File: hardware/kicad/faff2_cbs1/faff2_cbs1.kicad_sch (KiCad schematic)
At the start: 0 parts

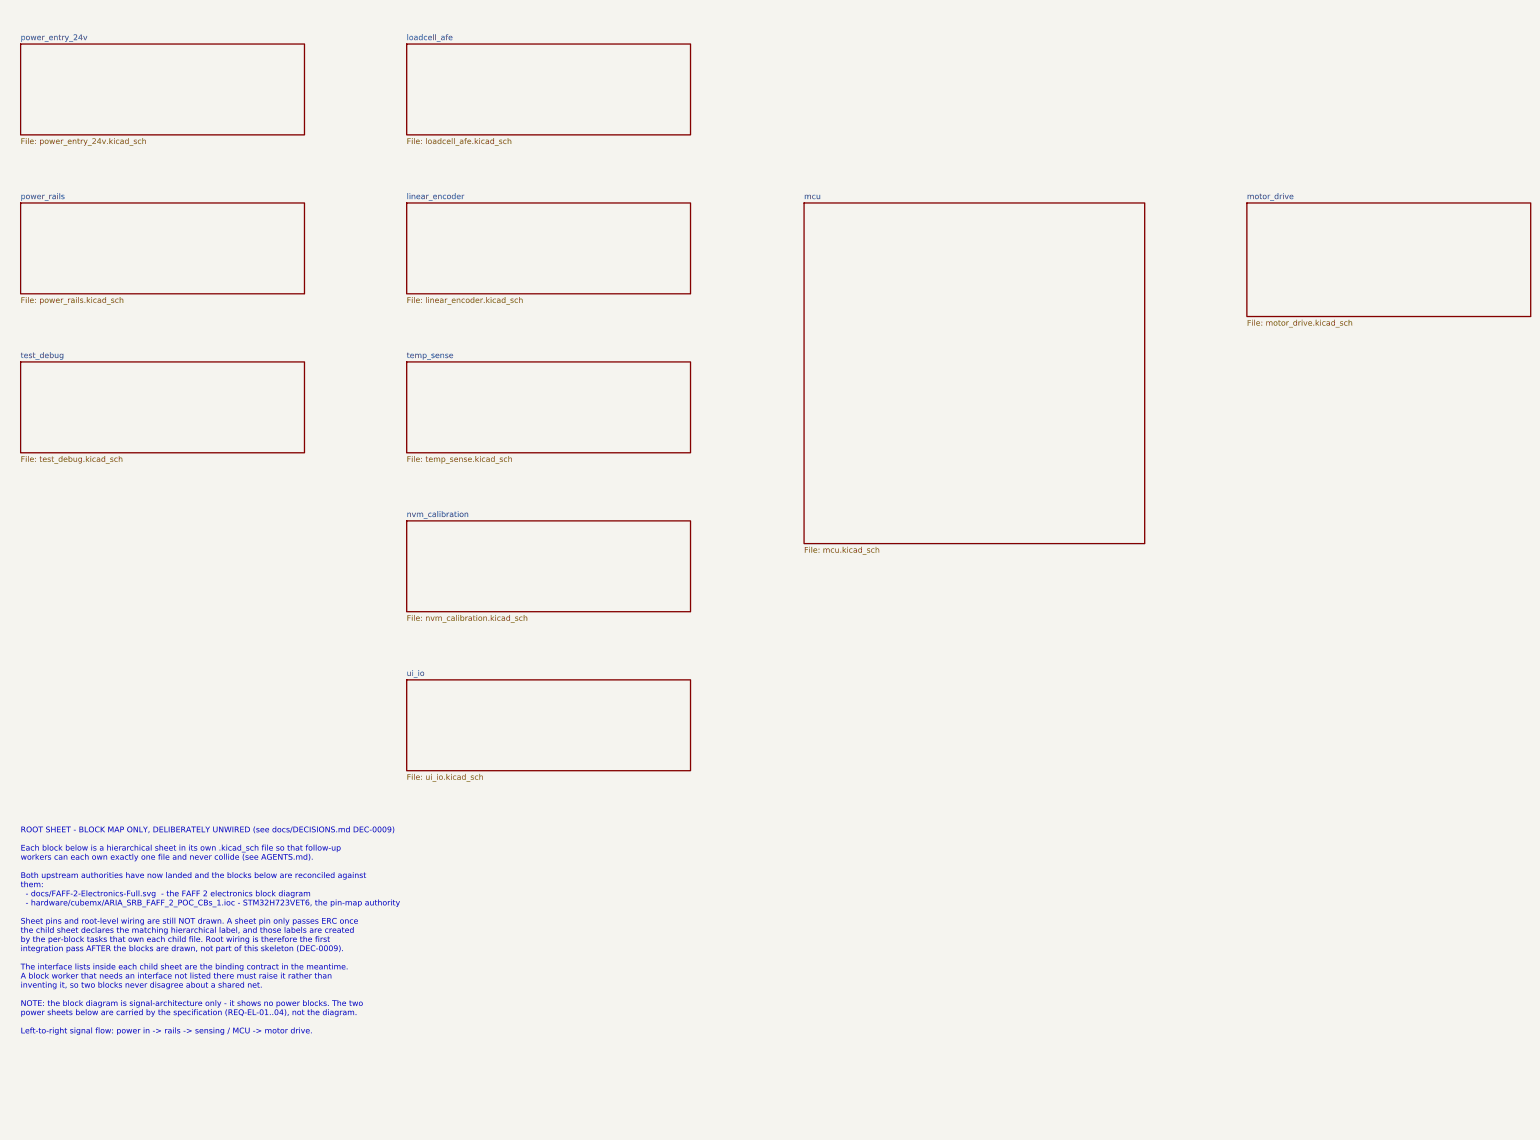
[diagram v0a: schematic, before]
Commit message: integrate: wire the root sheet - 113 sheet pins, 70 wires, ERC 0/0
Closes DEC-0009. Every net that crosses a block boundary is now drawn on
the root sheet: one sheet pin per hierarchical label a child declares,
each on a wire. Nothing on the root connects by name.

The layout is the block diagram of docs/FAFF-2-Electronics-Full.svg read
left to right - 24 V in top left, sensing and user I/O down the left
column, the MCU in the middle, motor drive on the right. Each peer
block's pin rows are aligned with the mcu rows they face, so all 48
mcu-to-peer nets are single straight wires with no bends and no
crossings.

Two topologies needed care:

  * power_entry_24v fans out to three different places. Its pins sit on
    a 5.08 mm pitch and the three routes are nested - V24_LOGIC straight
    across to power_rails, +24V_SW peeling down and running over the top
    of the mcu block to motor_drive, V24_MON dropping inside it - so no
    two cross.
  * the shared SPI2 CONFIG bus is tapped once per wire between
    motor_drive and temp_sense, which is why temp_sense sits under
    motor_drive rather than in the sensor column. The three taps and the
    ADS1120_nCS run are nested the same way: four junctions, zero
    crossings.

motor_drive declared CONFIG_SPI_MISO an output while temp_sense declared
it tri_state - the reconciliation actuator-sch-afe.md asked for at
integration. Both are tri_state now: three devices share that wire and
each drives it only while its own chip select is low.

Verification, whole project, nothing suppressed:
  ERC --severity-all          0 errors, 0 warnings (was 194 violations)
  netlist                     409 components, no duplicate references,
                              311 -> 253 nets, exactly the 58 merges the
                              113 pins over 55 net names predict
  overlap checker             root sheet clean; the 11 findings left in
                              linear_encoder / loadcell_afe / temp_sense
                     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
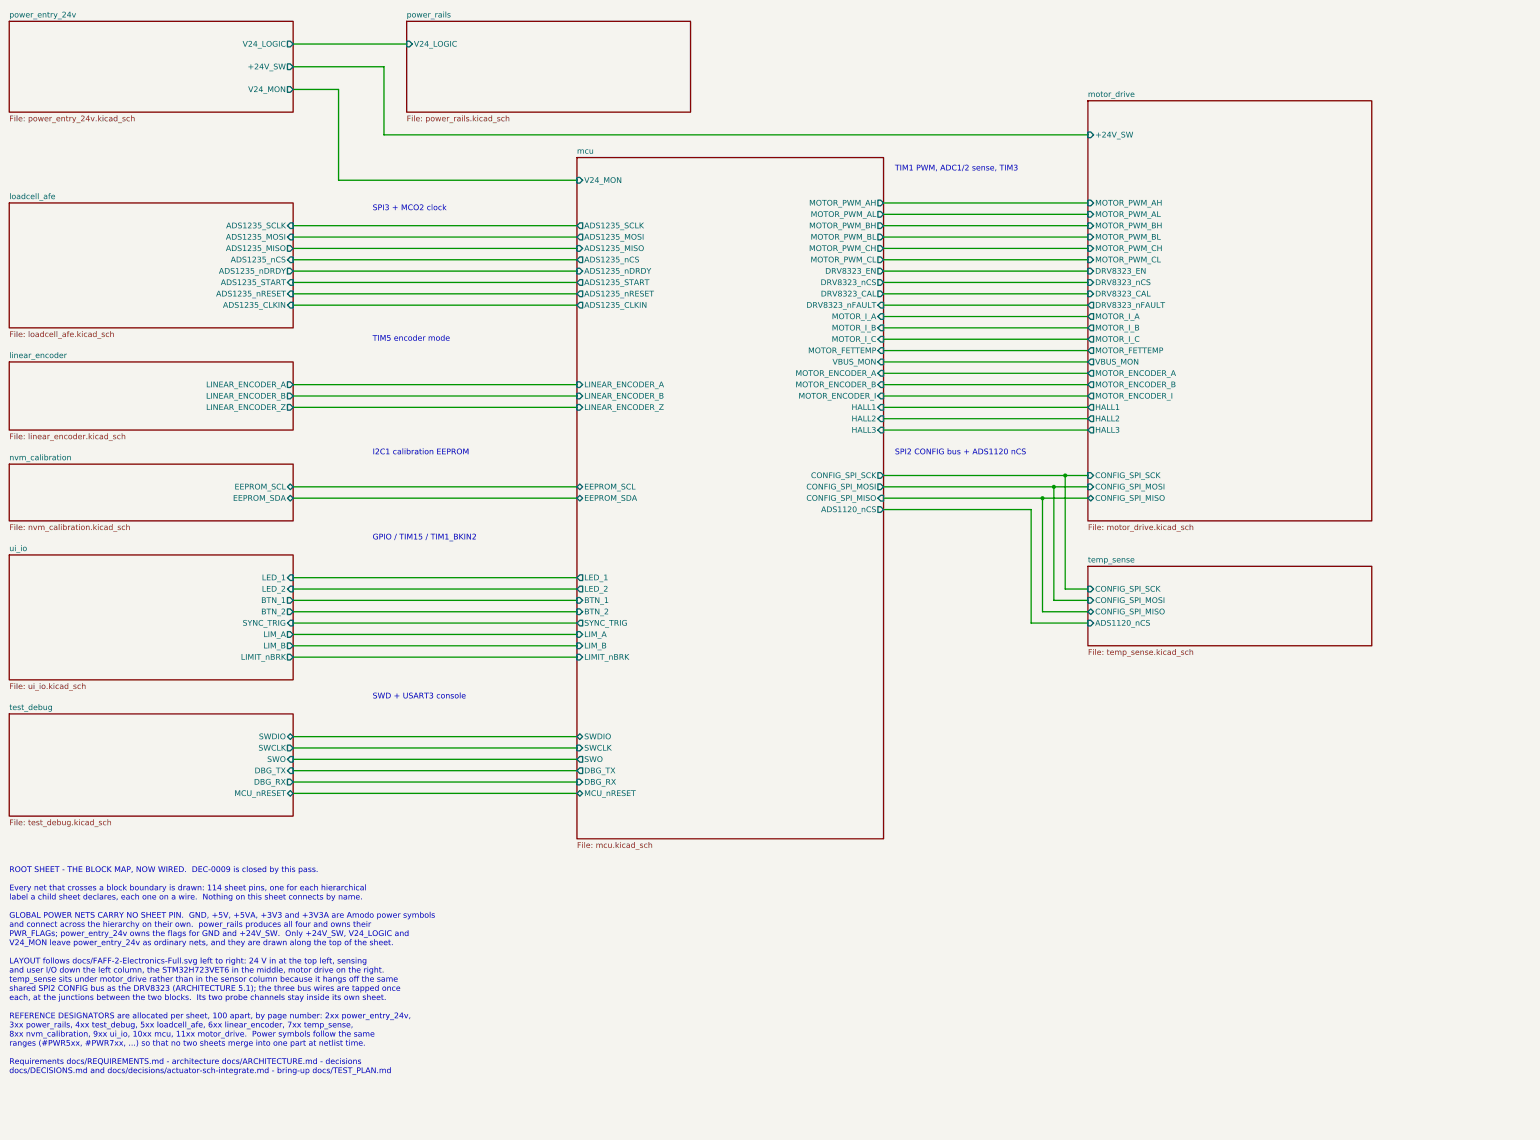
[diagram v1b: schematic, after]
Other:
- sheet linear_encoder ports: added LINEAR_ENCODER_A, LINEAR_ENCODER_B, LINEAR_ENCODER_Z; removed none
- sheet loadcell_afe ports: added ADS1235_CLKIN, ADS1235_MISO, ADS1235_MOSI, ADS1235_SCLK, ADS1235_START, ADS1235_nCS, ADS1235_nDRDY, ADS1235_nRESET; removed none
- sheet mcu ports: added ADS1120_nCS, ADS1235_CLKIN, ADS1235_MISO, ADS1235_MOSI, ADS1235_SCLK, ADS1235_START, ADS1235_nCS, ADS1235_nDRDY, ADS1235_nRESET, BTN_1, BTN_2, CONFIG_SPI_MISO, CONFIG_SPI_MOSI, CONFIG_SPI_SCK, DBG_RX, DBG_TX, DRV8323_CAL, DRV8323_EN, DRV8323_nCS, DRV8323_nFAULT, EEPROM_SCL, EEPROM_SDA, HALL1, HALL2, HALL3, LED_1, LED_2, LIMIT_nBRK, LIM_A, LIM_B, LINEAR_ENCODER_A, LINEAR_ENCODER_B, LINEAR_ENCODER_Z, MCU_nRESET, MOTOR_ENCODER_A, MOTOR_ENCODER_B, MOTOR_ENCODER_I, MOTOR_FETTEMP, MOTOR_I_A, MOTOR_I_B, MOTOR_I_C, MOTOR_PWM_AH, MOTOR_PWM_AL, MOTOR_PWM_BH, MOTOR_PWM_BL, MOTOR_PWM_CH, MOTOR_PWM_CL, SWCLK, SWDIO, SWO, SYNC_TRIG, V24_MON, VBUS_MON; removed none
- sheet motor_drive ports: added +24V_SW, CONFIG_SPI_MISO, CONFIG_SPI_MOSI, CONFIG_SPI_SCK, DRV8323_CAL, DRV8323_EN, DRV8323_nCS, DRV8323_nFAULT, HALL1, HALL2, HALL3, MOTOR_ENCODER_A, MOTOR_ENCODER_B, MOTOR_ENCODER_I, MOTOR_FETTEMP, MOTOR_I_A, MOTOR_I_B, MOTOR_I_C, MOTOR_PWM_AH, MOTOR_PWM_AL, MOTOR_PWM_BH, MOTOR_PWM_BL, MOTOR_PWM_CH, MOTOR_PWM_CL, VBUS_MON; removed none
- sheet nvm_calibration ports: added EEPROM_SCL, EEPROM_SDA; removed none
- sheet power_entry_24v ports: added +24V_SW, V24_LOGIC, V24_MON; removed none
- sheet power_rails ports: added V24_LOGIC; removed none
- sheet temp_sense ports: added ADS1120_nCS, CONFIG_SPI_MISO, CONFIG_SPI_MOSI, CONFIG_SPI_SCK; removed none
- sheet test_debug ports: added DBG_RX, DBG_TX, MCU_nRESET, SWCLK, SWDIO, SWO; removed none
- sheet ui_io ports: added BTN_1, BTN_2, LED_1, LED_2, LIMIT_nBRK, LIM_A, LIM_B, SYNC_TRIG; removed none
- note added: "GPIO / TIM15 / TIM1_BKIN2"
- note added: "I2C1 calibration EEPROM"
- note added: "ROOT SHEET - THE BLOCK MAP, NOW WIRED. DEC-0009 is closed by this pass. Every net that crosses a block boundary is drawn: 114 sheet pins, one for each hierarchical label a child sheet declares, each one on a wire. Nothing on this sheet connects by name. GLOBAL POWER NETS CARRY NO SHEET PIN. GND, +5V, +5VA, +3V3 and +3V3A are Amodo power symbols and connect across the hierarchy on their own. power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"
- note added: "SPI2 CONFIG bus + ADS1120 nCS"
- note added: "SPI3 + MCO2 clock"
- note added: "SWD + USART3 console"
- note added: "TIM1 PWM, ADC1/2 sense, TIM3"
- note added: "TIM5 encoder mode"
- note removed: "ROOT SHEET - BLOCK MAP ONLY, DELIBERATELY UNWIRED (see docs/DECISIONS.md DEC-0009) Each block below is a hierarchical sheet in its own .kicad_sch file so that follow-up workers can each own exactly one file and never collide (see AGENTS.md). Both upstream authorities have now landed and the blocks below are reconciled against them: - docs/FAFF-2-Electronics-Full.svg - the FAFF 2 electronics block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"

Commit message: review r1: dissolve test_debug into mcu, split the 24 MHz clock, A2 mcu, ui_io flow
Captain's review, three batches, all landing on mcu.kicad_sch so they ship together.

test_debug.kicad_sch is deleted. Its three blocks moved onto the sheet they serve:
H the SWD + USART3 debug header, J the rail probe header, K the GND hooks - all on
mcu, renumbered into the 10xx range (J401->J1003, R401/402->R1013/1014, J402->J1004,
TP401..406->TP1006..1011, #PWR401..414->#PWR1051..1064). The six SWD/USART3 nets were
shared only with mcu, so they are sheet-local labels now and their twelve sheet pins
came off the root. Nine blocks; pages renumber 2..10 and the refdes ranges become a
fixed table with 4xx retired. Standing rule written into AGENTS.md: test coverage
lives on the circuit page it covers, never its own sheet.

The shared 24 MHz reference is gone. The USB3320 gets its own crystal on REFCLK/XO
(Y1002 ECS-240-12-23G-JGN-TR, 27 pF C0G load caps sized from DS Table 4-11) in a new
block C; the STM32 keeps its own oscillator, minus R1004 and the fan-out. A bare
crystal on the STM32 is impossible without an .ioc change (PH1-OSC_OUT unallocated,
REQ-AR-16), so it stays a driven clock - the two domains now share nothing.

mcu is A2 and re-laid, and all 47 hierarchical labels are right-justified so the
names align outside the wire instead of running into the pin numbers. Net labels
left alone.

ui_io is graphical only, netlist byte-identical: R907 and R915 lie along the signal
(pre-rotated variants in the new faff2_passives.kicad_sym - never an instance
rotation), D903 shunts straight down, and the LIM_A / LIM_B exits are clear of the
+3V3 riser that ran through the LIM_A label.

Verified: ERC 0 errors / 0 warnings at --severity-all, nothing suppressed; netlist
equivalent net-for-net apart from the four rows of the authorised clock change;
411 components, 253 nets, all footprints resolving; overlap checker clean on every
sheet this branch touched. Review PDF deliberately not regene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
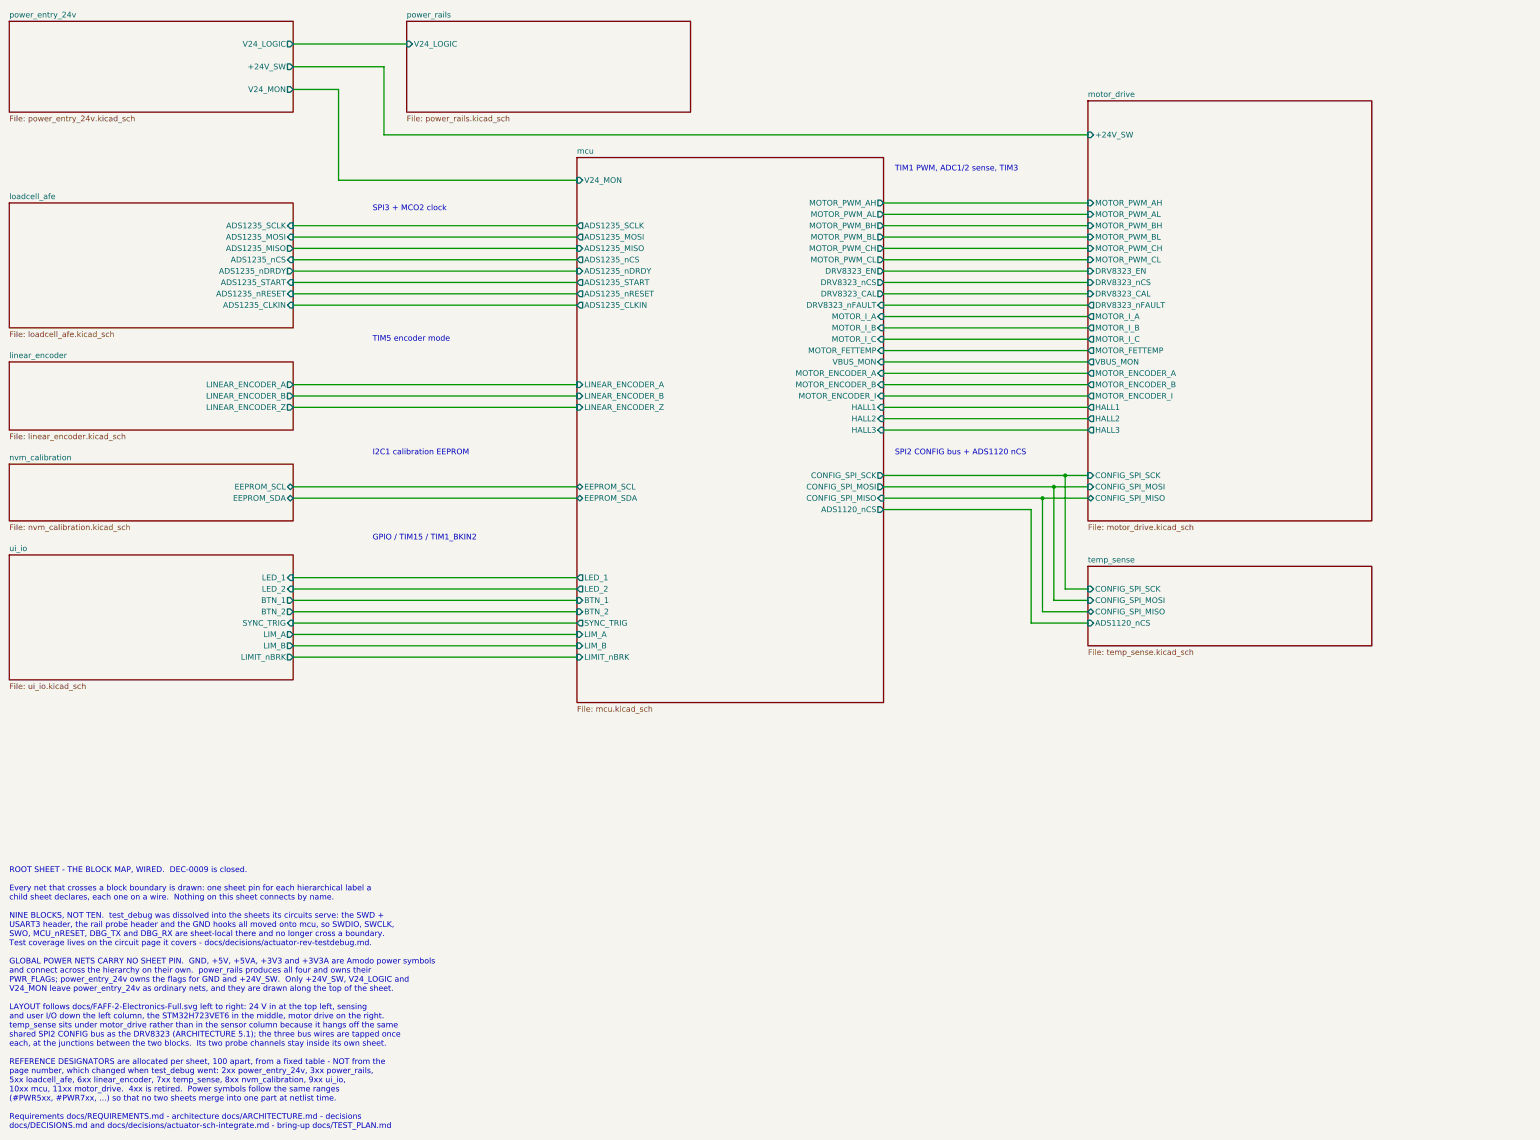
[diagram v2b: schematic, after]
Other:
- removed sheet test_debug
- sheet mcu ports: added none; removed DBG_RX, DBG_TX, MCU_nRESET, SWCLK, SWDIO, SWO
- note added: "ROOT SHEET - THE BLOCK MAP, WIRED. DEC-0009 is closed. Every net that crosses a block boundary is drawn: one sheet pin for each hierarchical label a child sheet declares, each one on a wire. Nothing on this sheet connects by name. NINE BLOCKS, NOT TEN. test_debug was dissolved into the sheets its circuits serve: the SWD + USART3 header, the rail probe header and the GND hooks all moved onto mcu, 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"
- note removed: "ROOT SHEET - THE BLOCK MAP, NOW WIRED. DEC-0009 is closed by this pass. Every net that crosses a block boundary is drawn: 114 sheet pins, one for each hierarchical label a child sheet declares, each one on a wire. Nothing on this sheet connects by name. GLOBAL POWER NETS CARRY NO SHEET PIN. GND, +5V, +5VA, +3V3 and +3V3A are Amodo power symbols and connect across the hierarchy on their own. power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"
- note removed: "SWD + USART3 console"
